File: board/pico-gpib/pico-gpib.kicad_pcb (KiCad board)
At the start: 2 copper layers, 65 x 35 mm, 7 parts, among them J1 GPIB, J2 USB_B_Micro, J3 RPI_GPIO, U2 SN75160BDW, U3 SN75162BDW

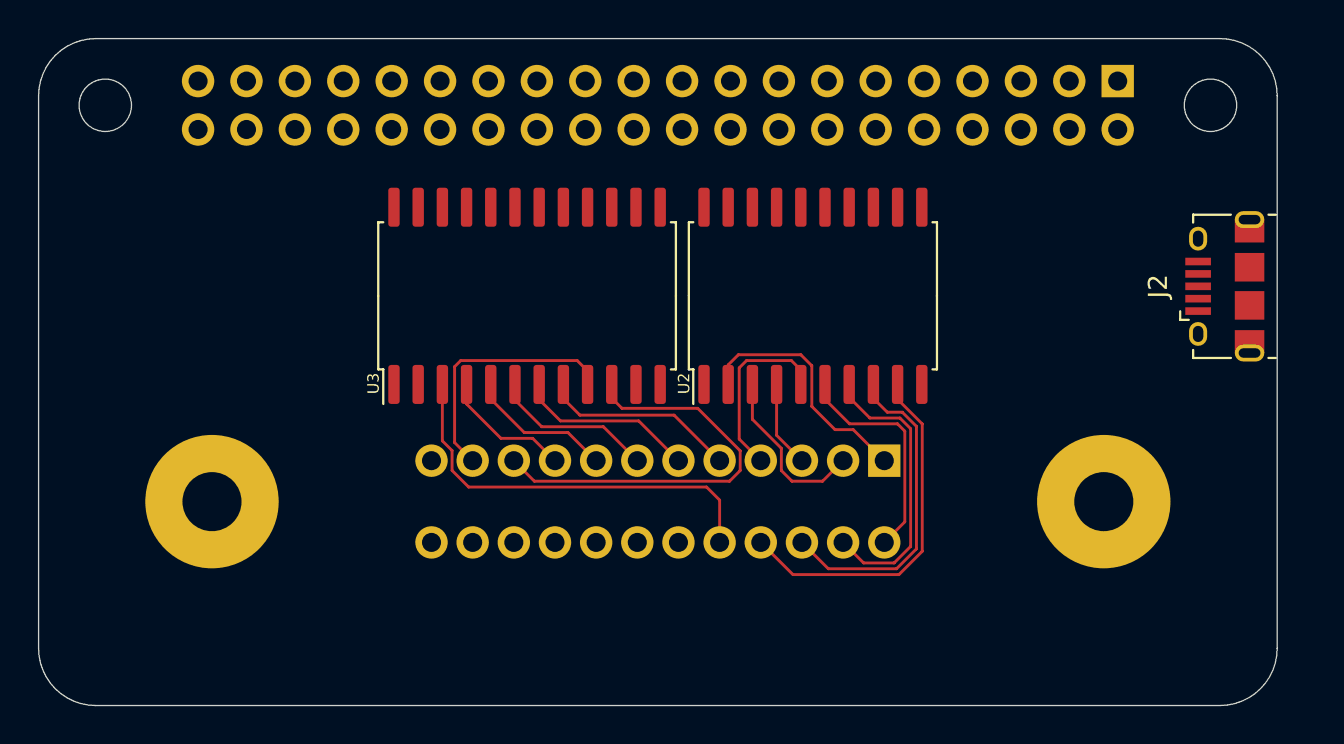
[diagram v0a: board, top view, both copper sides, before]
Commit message: Swap connectors to top of pico board.
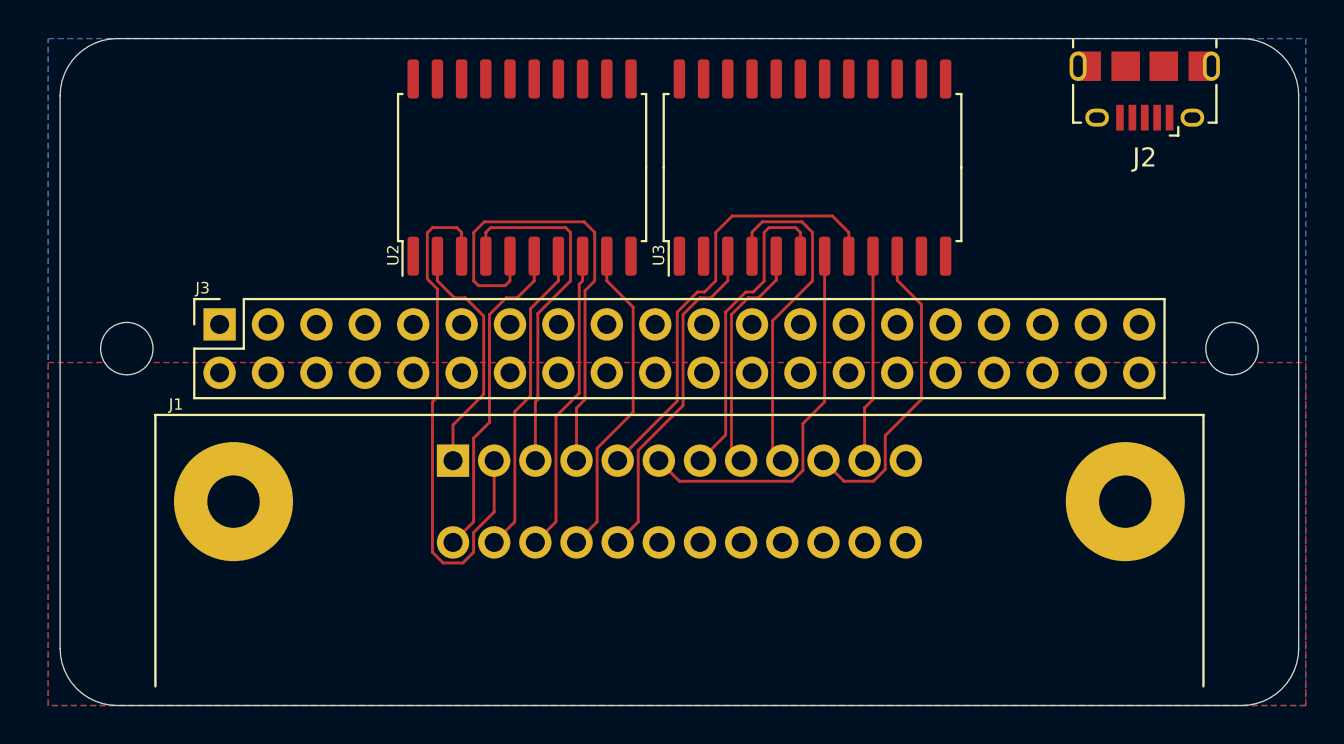
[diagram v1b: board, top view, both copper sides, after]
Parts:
- J1, J3: moved to F.Cu
- moved J3 48.8 mm to (127.0, 110.0)
- moved U2 16.7 mm to (142.9, 101.8)
- moved U3 16.4 mm to (158.1, 101.8)
- moved H1 12.8 mm to (122.1, 111.3)
- moved H2 12.8 mm to (180.1, 111.3)
- moved J2 11.1 mm to (175.6, 97.8), turned to 180 degrees
- moved J1 1.13 mm to (151.1, 130.0), turned to 0 degrees
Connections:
- J1 pad 12: Earth_Protective -> GND
- J1 pad PE: (no net) -> GND
- J2 pad 6: Earth_Protective -> GND
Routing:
- net /DIO2: track 9.07 -> 28.2 mm
- net /DIO4: track 9.69 -> 25.1 mm
- net /DIO3: track 4.55 -> 18.6 mm
- net /EOI: track 10.3 -> 23.3 mm
- net /IFC: track 6.90 -> 17.9 mm
- net /DAV: track 9.43 -> 20.0 mm
- net /NRFD: track 8.55 -> 17.0 mm
- net /SRQ: track 22.2 -> 16.4 mm
- net /DIO5: track 11.9 -> 17.1 mm
- net /NDAC: track 7.63 -> 12.2 mm
- net /REN: track 21.6 -> 17.8 mm
- net /ATN: track 13.4 -> 10.9 mm
- net /DIO8: track 19.0 -> 16.8 mm
- net /DIO6: track 15.1 -> 16.4 mm
- net /DIO7: track 17.0 -> 16.0 mm
- added copper zone on B.Cu, net GND
- added copper zone on F.Cu, net GND

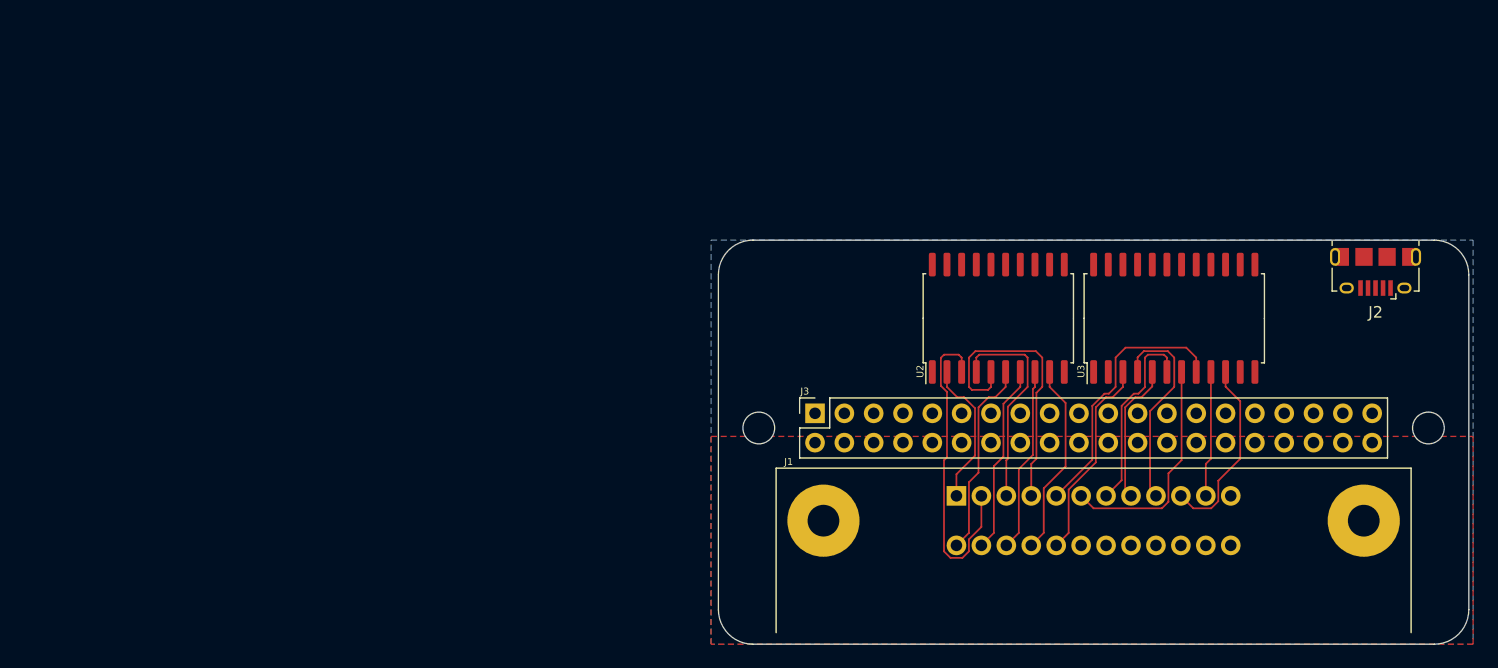
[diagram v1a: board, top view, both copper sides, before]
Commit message: Place and route most of the pico board.
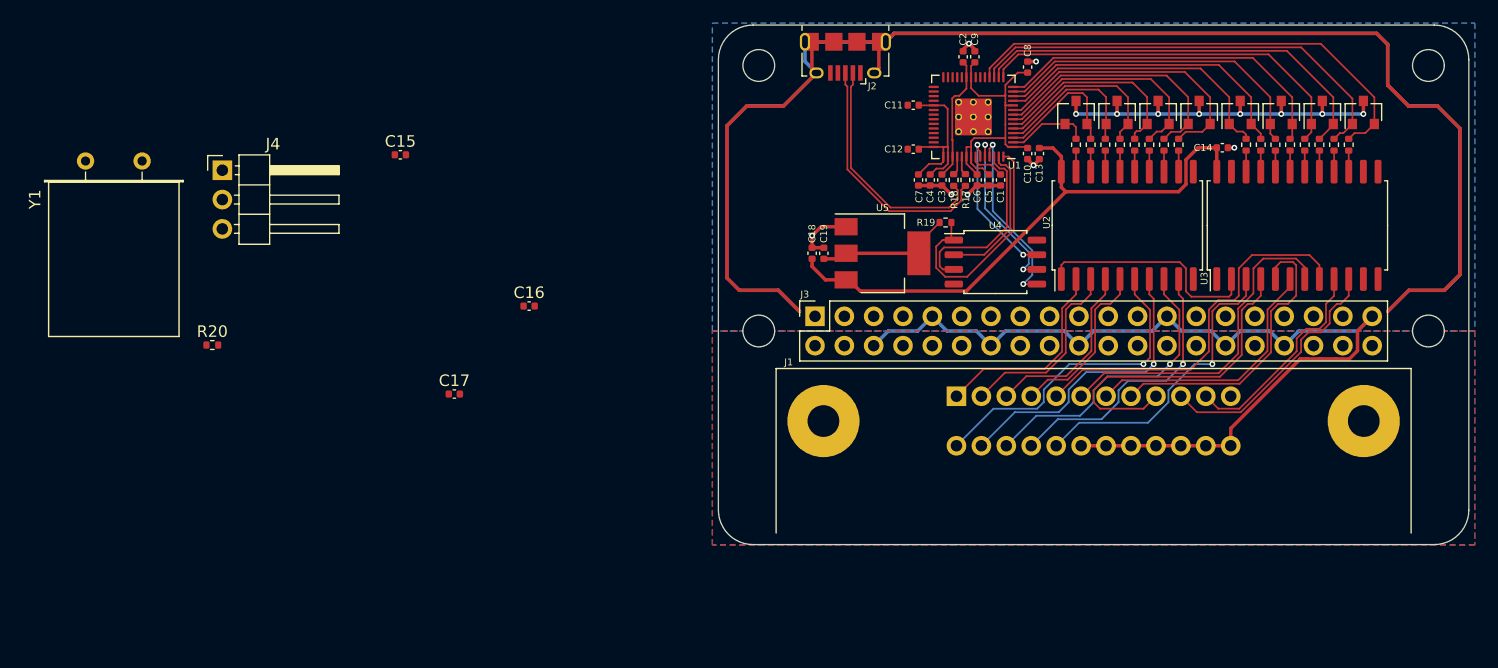
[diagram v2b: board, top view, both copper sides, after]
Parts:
- added C1: 100n, Capacitor_SMD:C_0402_1005Metric, F.Cu at (143.1, 89.8)
- added C10: 100n, Capacitor_SMD:C_0402_1005Metric, F.Cu at (145.4, 87.5)
- added C11: 100n, Capacitor_SMD:C_0402_1005Metric, F.Cu at (135.5, 83.3)
- added C12: 100n, Capacitor_SMD:C_0402_1005Metric, F.Cu at (135.5, 87.1)
- added C13: 100n, Capacitor_SMD:C_0402_1005Metric, F.Cu at (146.4, 87.5)
- added C14: 100n, Capacitor_SMD:C_0402_1005Metric, F.Cu at (162.3, 87.0)
- added C15: 100n, Capacitor_SMD:C_0402_1005Metric, F.Cu at (91.1, 87.6)
- added C16: 27p, Capacitor_SMD:C_0402_1005Metric, F.Cu at (102.2, 100.7)
- added C17: 27p, Capacitor_SMD:C_0402_1005Metric, F.Cu at (95.8, 108.3)
- added C18: 10u, Capacitor_SMD:C_0402_1005Metric, F.Cu at (126.7, 96.1)
- added C19: 10u, Capacitor_SMD:C_0402_1005Metric, F.Cu at (127.8, 96.1)
- added C2: 100n, Capacitor_SMD:C_0402_1005Metric, F.Cu at (139.8, 79.1)
- added C3: 1u, Capacitor_SMD:C_0402_1005Metric, F.Cu at (138.0, 89.8)
- added C4: 1u, Capacitor_SMD:C_0402_1005Metric, F.Cu at (137.0, 89.8)
- added C5: 100n, Capacitor_SMD:C_0402_1005Metric, F.Cu at (142.1, 89.8)
- added C6: 100n, Capacitor_SMD:C_0402_1005Metric, F.Cu at (141.0, 89.8)
- added C7: 100n, Capacitor_SMD:C_0402_1005Metric, F.Cu at (136.0, 89.8)
- added C8: 100n, Capacitor_SMD:C_0402_1005Metric, F.Cu at (145.4, 80.0)
- added C9: 100n, Capacitor_SMD:C_0402_1005Metric, F.Cu at (140.8, 79.1)
- added D1: D_Schottky_x2_KCom_AAK_Split, Package_TO_SOT_SMD:SOT-23, F.Cu at (149.6, 83.9)
- added D2: D_Schottky_x2_KCom_AAK_Split, Package_TO_SOT_SMD:SOT-23, F.Cu at (153.2, 83.9)
- added D3: D_Schottky_x2_KCom_AAK_Split, Package_TO_SOT_SMD:SOT-23, F.Cu at (156.7, 83.9)
- added D4: D_Schottky_x2_KCom_AAK_Split, Package_TO_SOT_SMD:SOT-23, F.Cu at (160.3, 83.9)
- added D5: D_Schottky_x2_KCom_AAK_Split, Package_TO_SOT_SMD:SOT-23, F.Cu at (163.8, 83.9)
- added D6: D_Schottky_x2_KCom_AAK_Split, Package_TO_SOT_SMD:SOT-23, F.Cu at (167.4, 83.9)
- added D7: D_Schottky_x2_KCom_AAK_Split, Package_TO_SOT_SMD:SOT-23, F.Cu at (170.9, 83.9)
- added D8: D_Schottky_x2_KCom_AAK_Split, Package_TO_SOT_SMD:SOT-23, F.Cu at (174.5, 83.9)
- added H1: MountingHole, local:MountingHole_RPi_HAT, F.Cu at (180.1, 79.9)
- added H1: MountingHole, local:MountingHole_RPi_HAT, F.Cu at (122.1, 102.9)
- added J4: Debug, Connector_PinHeader_2.54mm:PinHeader_1x03_P2.54mm_Horizontal, F.Cu at (75.7, 88.9)
- added R1: R, Resistor_SMD:R_0402_1005Metric, F.Cu at (149.6, 86.7)
- added R10: R, Resistor_SMD:R_0402_1005Metric, F.Cu at (165.6, 86.7)
- added R11: R, Resistor_SMD:R_0402_1005Metric, F.Cu at (166.9, 86.7)
- added R12: R, Resistor_SMD:R_0402_1005Metric, F.Cu at (168.1, 86.7)
- added R13: R, Resistor_SMD:R_0402_1005Metric, F.Cu at (169.4, 86.7)
- added R14: R, Resistor_SMD:R_0402_1005Metric, F.Cu at (170.7, 86.7)
- added R15: R, Resistor_SMD:R_0402_1005Metric, F.Cu at (172.0, 86.7)
- added R16: R, Resistor_SMD:R_0402_1005Metric, F.Cu at (173.2, 86.7)
- added R17: 27R4, Resistor_SMD:R_0402_1005Metric, F.Cu at (140.0, 89.8)
- added R18: 27R4, Resistor_SMD:R_0402_1005Metric, F.Cu at (139.0, 89.8)
- added R19: 10k, Resistor_SMD:R_0402_1005Metric, F.Cu at (138.3, 93.5)
- added R2: R, Resistor_SMD:R_0402_1005Metric, F.Cu at (150.9, 86.7)
- added R20: 1k, Resistor_SMD:R_0402_1005Metric, F.Cu at (74.8, 104.1)
- added R3: R, Resistor_SMD:R_0402_1005Metric, F.Cu at (152.1, 86.7)
- added R4: R, Resistor_SMD:R_0402_1005Metric, F.Cu at (153.4, 86.7)
- added R5: R, Resistor_SMD:R_0402_1005Metric, F.Cu at (154.7, 86.7)
- added R6: R, Resistor_SMD:R_0402_1005Metric, F.Cu at (156.0, 86.7)
- added R7: R, Resistor_SMD:R_0402_1005Metric, F.Cu at (157.2, 86.7)
- added R8: R, Resistor_SMD:R_0402_1005Metric, F.Cu at (158.5, 86.7)
- added R9: R, Resistor_SMD:R_0402_1005Metric, F.Cu at (164.3, 86.7)
- added U1: RP2040, local:RP2040-QFN-56, F.Cu at (140.7, 84.3)
- added U4: W25Q128JVS, Package_SO:SOIC-8_5.23x5.23mm_P1.27mm, F.Cu at (142.6, 96.9)
- added U5: NCP1117-3.3, Package_TO_SOT_SMD:SOT-223-3_TabPin2, F.Cu at (132.8, 96.1)
- added Y1: ABLS-12.000MHZ-20-B-3-H-T, Crystal:Crystal_HC49-U_Horizontal, F.Cu at (63.8, 88.1)
- moved J2 49.6 mm to (129.6, 79.1)
- moved H1 31.4 mm to (122.1, 79.9)
- moved U2 13.8 mm to (154.1, 93.7)
- moved U3 13.4 mm to (168.8, 93.7)
- moved J1 8.63 mm to (151.1, 121.4)
- moved J3 8.40 mm to (127.0, 101.6)
- moved H2 8.40 mm to (180.1, 102.9)
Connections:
- net /ATN renamed /Bus/B_ATN
- net /DAV renamed /Bus/B_DAV
- net /DIO1 renamed /Bus/B_DIO1
- net /DIO2 renamed /Bus/B_DIO2
- net /DIO3 renamed /Bus/B_DIO3
- net /DIO4 renamed /Bus/B_DIO4
- net /DIO5 renamed /Bus/B_DIO5
- net /DIO6 renamed /Bus/B_DIO6
- net /DIO7 renamed /Bus/B_DIO7
- net /DIO8 renamed /Bus/B_DIO8
- net /EOI renamed /Bus/B_EOI
- net /IFC renamed /Bus/B_IFC
- net /NDAC renamed /Bus/B_~DAC
- net /NRFD renamed /Bus/B_~RFD
- net /REN renamed /Bus/B_REN
- net /SRQ renamed /Bus/B_SRQ
- net Net-(J2-Pad1) renamed VBUS
- J1 pad 12: GND -> Earth_Protective
- J1 pad PE: GND -> (no net)
- J2 pad 2: Net-(J2-Pad2) -> /USB_D-
- J2 pad 3: Net-(J2-Pad3) -> /USB_D+
- J2 pad 6: GND -> Earth_Protective
- U2 pad 1: Net-(U2-Pad1) -> /TE
- U2 pad 11: Net-(U2-Pad11) -> /~PE
- U2 pad 12: Net-(U2-Pad12) -> /Bus/I_DIO8
- U2 pad 13: Net-(U2-Pad13) -> /Bus/I_DIO7
- U2 pad 14: Net-(U2-Pad14) -> /Bus/I_DIO6
- U2 pad 15: Net-(U2-Pad15) -> /Bus/I_DIO5
- U2 pad 16: Net-(U2-Pad16) -> /Bus/I_DIO4
- U2 pad 17: Net-(U2-Pad17) -> /Bus/I_DIO3
- U2 pad 18: Net-(U2-Pad18) -> /Bus/I_DIO2
- U2 pad 19: Net-(U2-Pad19) -> /Bus/I_DIO1
- U3 pad 1: Net-(U3-Pad1) -> /SC
- U3 pad 13: Net-(U3-Pad13) -> /DC
- U3 pad 15: Net-(U3-Pad15) -> /Bus/I_SRQ
- U3 pad 16: Net-(U3-Pad16) -> /Bus/I_ATN
- U3 pad 17: Net-(U3-Pad17) -> /Bus/I_EOI
- U3 pad 18: Net-(U3-Pad18) -> /Bus/I_DAV
- U3 pad 19: Net-(U3-Pad19) -> /Bus/I_~RFD
- U3 pad 2: Net-(U3-Pad2) -> /TE
- U3 pad 20: Net-(U3-Pad20) -> /Bus/I_~DAC
- U3 pad 21: Net-(U3-Pad21) -> /Bus/I_IFC
- U3 pad 22: Net-(U3-Pad22) -> /Bus/I_REN
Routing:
- net Earth_Protective: track 0.00 -> 234.4 mm
- net GND: track 0.00 -> 98.5 mm, vias 0 -> 7
- net +3V3: track 0.00 -> 53.6 mm
- net +5V: track 0.00 -> 50.5 mm
- net /SRQ: track 0.00 -> 42.0 mm
- net /ATN: track 0.00 -> 38.7 mm
- net /EOI: track 0.00 -> 36.1 mm
- net +2V5: track 0.00 -> 34.0 mm, vias 0 -> 8
- net /DAV: track 0.00 -> 33.3 mm
- net /~RFD: track 0.00 -> 30.3 mm
- net /~DAC: track 0.00 -> 28.4 mm
- net /IFC: track 0.00 -> 26.8 mm
- net /REN: track 0.00 -> 25.4 mm
- net /DIO8: track 0.00 -> 24.9 mm
- net /DIO7: track 0.00 -> 22.3 mm
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- added copper zone on B.Cu, net Earth_Protective
- added copper zone on F.Cu, net Earth_Protective
- removed copper zone on F.Cu, net GND
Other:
- board size 65 x 35 mm -> 65 x 45 mm

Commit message: Rotate RP2040 to fit in crystal.
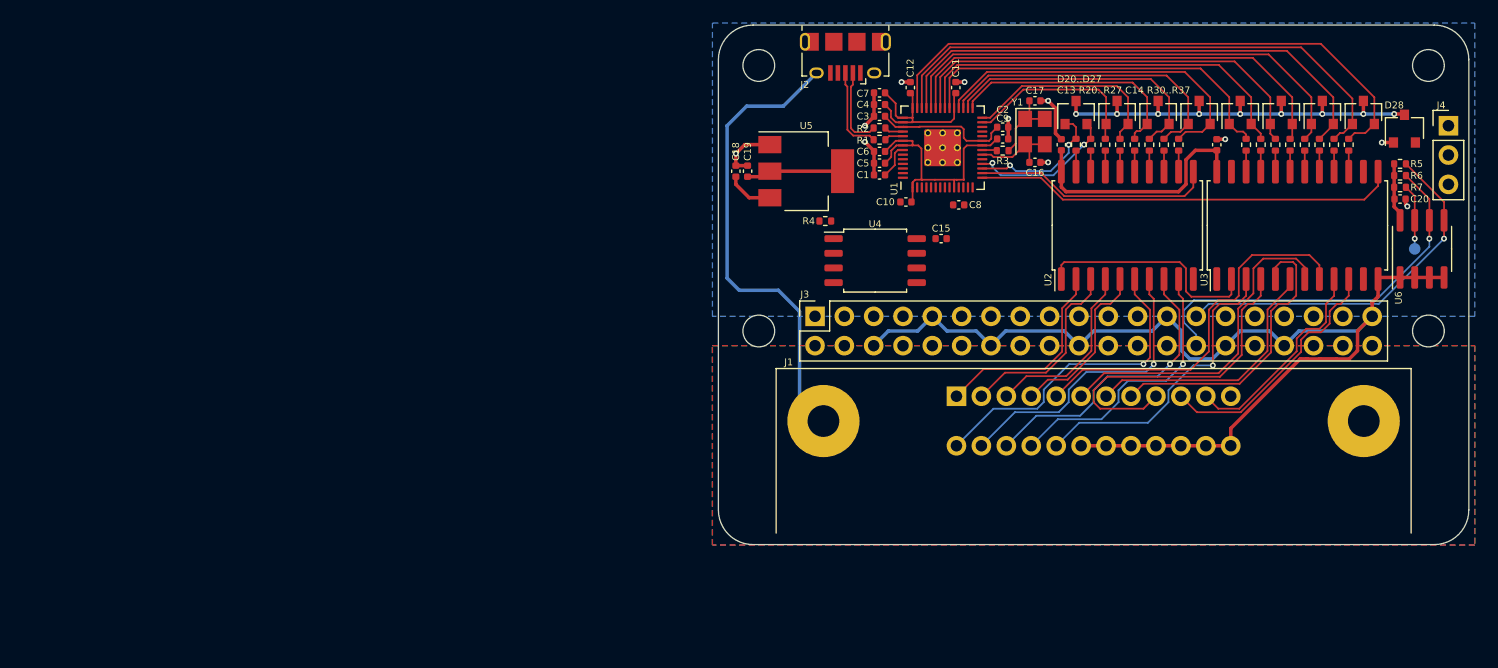
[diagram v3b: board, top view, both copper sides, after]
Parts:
- removed D1: D_Schottky_x2_KCom_AAK_Split, Package_TO_SOT_SMD:SOT-23
- removed the R1 at (149.6, 86.7)
- added C20: 100n, Capacitor_SMD:C_0402_1005Metric, F.Cu at (177.7, 91.4)
- added D20: BAT54C, Package_TO_SOT_SMD:SOT-23, F.Cu at (149.6, 83.9)
- added D28: MMBZ5222BLT1G, Package_TO_SOT_SMD:SC-59, F.Cu at (178.1, 85.3)
- added R3: 1k, Resistor_SMD:R_0402_1005Metric, F.Cu at (143.3, 87.2)
- added R5: 3k9, Resistor_SMD:R_0402_1005Metric, F.Cu at (177.7, 88.4)
- added R6: 3k9, Resistor_SMD:R_0402_1005Metric, F.Cu at (177.7, 89.4)
- added R7: 1k, Resistor_SMD:R_0402_1005Metric, F.Cu at (177.7, 90.4)
- added TP1: TestPoint, TestPoint:TestPoint_Pad_D1.0mm, B.Cu at (178.9, 95.8)
- added U6: CAT24C32, Package_SO:SOIC-8_3.9x4.9mm_P1.27mm, F.Cu at (179.6, 95.8)
- C16, C17: value 27p -> 10p
- D21: renamed from D2; value D_Schottky_x2_KCom_AAK_Split -> BAT54C
- D22: renamed from D3; value D_Schottky_x2_KCom_AAK_Split -> BAT54C
- D23: renamed from D4; value D_Schottky_x2_KCom_AAK_Split -> BAT54C
- D24: renamed from D5; value D_Schottky_x2_KCom_AAK_Split -> BAT54C
- D25: renamed from D6; value D_Schottky_x2_KCom_AAK_Split -> BAT54C
- D26: renamed from D7; value D_Schottky_x2_KCom_AAK_Split -> BAT54C
- D27: renamed from D8; value D_Schottky_x2_KCom_AAK_Split -> BAT54C
- J4: footprint Connector_PinHeader_2.54mm:PinHeader_1x03_P2.54mm_Horizontal -> Connector_PinHeader_2.54mm:PinHeader_1x03_P2.54mm_Vertical
- R20: value 1k -> R
- Y1: value ABLS-12.000MHZ-20-B-3-H-T -> 12M10PI/XT324-10/20; footprint Crystal:Crystal_HC49-U_Horizontal -> Crystal:Crystal_SMD_3225-4Pin_3.2x2.5mm
- moved J4 106.3 mm to (181.9, 85.1)
- moved Y1 82.3 mm to (146.1, 85.6), turned to 270 degrees
- moved R20 76.8 mm to (149.6, 86.7), turned to 90 degrees
- moved C17 56.3 mm to (146.1, 82.9)
- moved C15 47.4 mm to (137.9, 94.9)
- moved C16 45.5 mm to (146.1, 88.3)
- moved C8 13.3 mm to (139.4, 91.9), turned to 0 degrees
- moved C10 11.3 mm to (134.9, 91.7), turned to 180 degrees
- moved C1 10.5 mm to (132.6, 89.4), turned to 180 degrees
- moved U4 10.4 mm to (132.2, 96.8)
- moved R4 10.4 mm to (127.9, 93.3)
- moved U5 9.71 mm to (126.2, 89.0)
- moved C18 9.71 mm to (120.1, 89.0)
- moved C19 9.71 mm to (121.2, 89.0)
- moved C5 9.58 mm to (132.6, 88.3), turned to 180 degrees
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- renumbered R17 to R1, R18 to R2, R2 to R21, R3 to R22, R4 to R23, R5 to R24, R6 to R25, R7 to R26, R8 to R27, R9 to R30, R10 to R31, R11 to R32, R12 to R33, R13 to R34, R14 to R35, R15 to R36, R16 to R37, R19 to R4
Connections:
- J3 pad 27: Net-(J3-Pad27) -> /ID_SD
- J3 pad 28: Net-(J3-Pad28) -> /ID_SC
- J3 pad 4: Net-(J3-Pad4) -> Net-(J3-Pad2)
- R20 pad 1: Net-(R20-Pad1) -> /Bus/I_DIO1
- R20 pad 2: Net-(C17-Pad1) -> /DIO1
- U1 pad 11: /REN -> Net-(U1-Pad11)
- U1 pad 12: /IFC -> Net-(U1-Pad12)
- U1 pad 13: /~DAC -> /TE
- U1 pad 14: /~RFD -> /SC
- U1 pad 15: /DAV -> /DC
- U1 pad 16: /EOI -> /~PE
- U1 pad 17: /ATN -> /DIO1
- U1 pad 18: /SRQ -> /DIO2
- U1 pad 2: /DIO1 -> Net-(U1-Pad2)
- U1 pad 21: Net-(R20-Pad1) -> Net-(R3-Pad1)
- U1 pad 27: /TE -> /DIO3
- U1 pad 28: /SC -> /DIO4
- U1 pad 29: /DC -> /DIO5
- U1 pad 3: /DIO2 -> Net-(U1-Pad3)
- U1 pad 30: /~PE -> /DIO6
- U1 pad 31: Net-(U1-Pad31) -> /DIO7
- U1 pad 32: Net-(U1-Pad32) -> /DIO8
- U1 pad 34: Net-(U1-Pad34) -> /REN
- U1 pad 35: Net-(U1-Pad35) -> /IFC
- U1 pad 36: Net-(U1-Pad36) -> /~DAC
- U1 pad 37: Net-(U1-Pad37) -> /~RFD
- U1 pad 38: Net-(U1-Pad38) -> /DAV
- U1 pad 39: Net-(U1-Pad39) -> /EOI
- U1 pad 4: /DIO3 -> Net-(U1-Pad4)
- U1 pad 40: Net-(U1-Pad40) -> /ATN
- U1 pad 41: Net-(U1-Pad41) -> /SRQ
- U1 pad 5: /DIO4 -> Net-(U1-Pad5)
- U1 pad 6: /DIO5 -> Net-(U1-Pad6)
- U1 pad 7: /DIO6 -> Net-(U1-Pad7)
- U1 pad 8: /DIO7 -> Net-(U1-Pad8)
- U1 pad 9: /DIO8 -> Net-(U1-Pad9)
- Y1 pad 1: Net-(C16-Pad1) -> Net-(C17-Pad1)
- Y1 pad 2: Net-(C17-Pad1) -> Net-(C16-Pad1)
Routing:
- net Earth_Protective: track 234.4 -> 40.7 mm
- net /DC: track 0.00 -> 36.8 mm
- net /ID_SC: track 0.00 -> 34.1 mm, vias 0 -> 1
- net /ID_SD: track 0.00 -> 32.1 mm, vias 0 -> 1
- net +5V: track 50.5 -> 25.5 mm
- net /FLASH_~CS: track 20.9 -> 0.00 mm
- net /~PE: track 0.00 -> 20.8 mm
- net GND: track 98.5 -> 116.0 mm, vias 7 -> 11
- net /FLASH_D0: track 16.1 -> 0.00 mm, vias 2 -> 0
- net /FLASH_D2: track 16.1 -> 0.00 mm
- net /FLASH_CLK: track 14.8 -> 0.00 mm, vias 2 -> 0
- net /USB_D+: track 21.6 -> 7.63 mm
- net /FLASH_D3: track 13.5 -> 0.00 mm, vias 2 -> 0
- net /USB_D-: track 20.6 -> 7.12 mm
- net /FLASH_D1: track 12.7 -> 0.00 mm
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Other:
- board text added: "D20..D27 C13 R20..R27 C14 R30..R37"
